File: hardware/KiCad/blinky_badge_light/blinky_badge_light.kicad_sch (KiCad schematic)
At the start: 14 parts, among them U1 ESP32-S3-WROOM-1

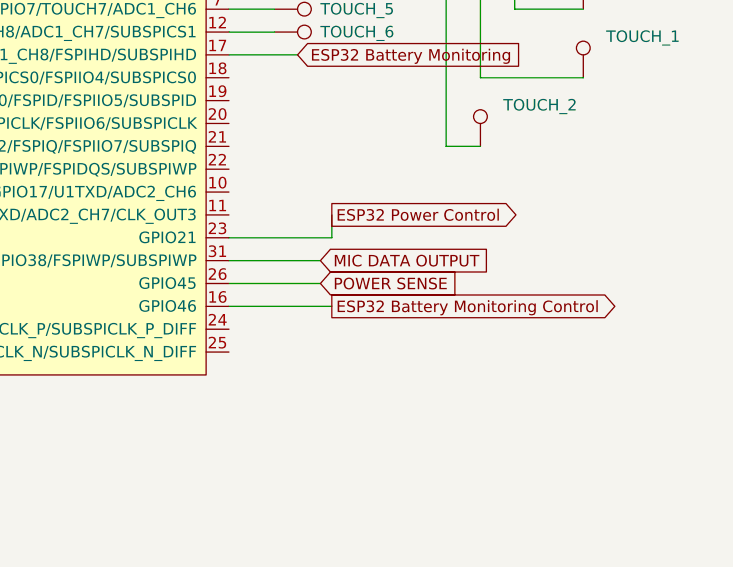
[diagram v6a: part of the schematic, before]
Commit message: much more complicated button logic now
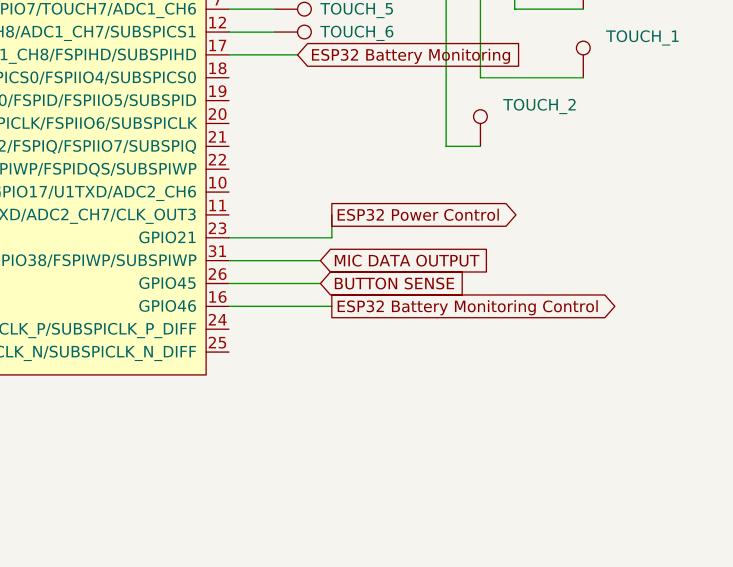
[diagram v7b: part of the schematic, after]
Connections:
- net POWER SENSE renamed BUTTON SENSE
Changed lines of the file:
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@@
 		)
 	)
-	(global_label "POWER SENSE"
+	(global_label "BUTTON SENSE"
 		(shape input)
 		(at 201.93 123.19 0)
